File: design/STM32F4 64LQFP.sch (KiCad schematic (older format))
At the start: 15 parts, among them P2 SWD, U1 STM32F40X_LQFP64, X2 8MHz 10ppm

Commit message: Saved project with more recent version of KiCad. Added IRS2184 half bridge driver to BLDC_4_cache.lib
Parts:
- C10, C11, C12, C13, C14, C15, C16, C17, C31, C32, C35, C38: symbol C -> C-RESCUE-BLDC_4
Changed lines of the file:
@@
 EESchema Schematic File Version 2
+LIBS:BLDC_4-rescue
 LIBS:power
 LIBS:device
@@
 LIBS:crf_1
 LIBS:BLDC_4-cache
-EELAYER 24 0
+EELAYER 25 0
 EELAYER END
 $Descr A4 11693 8268
@@
 $EndComp
 $Comp
-L C C17
+L C-RESCUE-BLDC_4 C17
 U 1 1 53F757AE
 P 7500 6350
@@
 $EndComp
 $Comp
-L C C16
+L C-RESCUE-BLDC_4 C16
 U 1 1 53F757B5
 P 7500 6100
@@
 $EndComp
 $Comp
-L GND #PWR035
+L GND-RESCUE-BLDC_4 #PWR035
 U 1 1 53F757BC
 P 8000 6050
@@
 $EndComp
 $Comp
-L GND #PWR037
+L GND-RESCUE-BLDC_4 #PWR037
 U 1 1 53F757C8
 P 7200 5150
@@
 $EndComp
 $Comp
-L C C15
+L C-RESCUE-BLDC_4 C15
 U 1 1 53F757DB
 P 7350 1800
@@
 $EndComp
 $Comp
-L C C38
+L C-RESCUE-BLDC_4 C38
 U 1 1 53F757E2
 P 8100 1800
@@
 $EndComp
 $Comp
-L GND #PWR039
+L GND-RESCUE-BLDC_4 #PWR039
 U 1 1 53F757E9
 P 8250 1600
@@
 $EndComp
 $Comp
-L GND #PWR040
+L GND-RESCUE-BLDC_4 #PWR040
 U 1 1 53F757EF
 P 7150 2550
@@
 SWCLK
 $Comp
-L C C31
+L C-RESCUE-BLDC_4 C31
 U 1 1 53F757F8
 P 7750 5450
@@
 $EndComp
 $Comp
-L C C35
+L C-RESCUE-BLDC_4 C35
 U 1 1 53F757FF
 P 8000 5450
@@
 NoConn ~ 4500 5450
 $Comp
-L GND #PWR042
+L GND-RESCUE-BLDC_4 #PWR042
 U 1 1 53F75856
 P 7950 3300
@@
 	7750 6350 7700 6350
 $Comp
-L C C32
+L C-RESCUE-BLDC_4 C32
 U 1 1 53F75896
 P 7950 3100
@@
 $EndComp
 $Comp
-L GND #PWR044
+L GND-RESCUE-BLDC_4 #PWR044
 U 1 1 53F7741D
 P 9600 3100
@@
 NRST
 $Comp
-L C C10
+L C-RESCUE-BLDC_4 C10
 U 1 1 53F77426
 P 9400 1300
@@
 $EndComp
 $Comp
-L C C11
+L C-RESCUE-BLDC_4 C11
 U 1 1 53F7742D
 P 9650 1300
@@
 $EndComp
 $Comp
-L C C14
+L C-RESCUE-BLDC_4 C14
 U 1 1 53F77434
 P 10400 1300
@@
 $EndComp
 $Comp
-L GND #PWR045
+L GND-RESCUE-BLDC_4 #PWR045
 U 1 1 53F7743B
 P 9100 1650
@@
 $EndComp
 $Comp
-L C C12
+L C-RESCUE-BLDC_4 C12
 U 1 1 53F77447
 P 9900 1300
@@
 $EndComp
 $Comp
-L C C13
+L C-RESCUE-BLDC_4 C13
 U 1 1 53F7744E
 P 10150 1300
@@
 $EndComp
 $Comp
-L GND #PWR047
+L GND-RESCUE-BLDC_4 #PWR047
 U 1 1 54097D19
 P 7750 2150

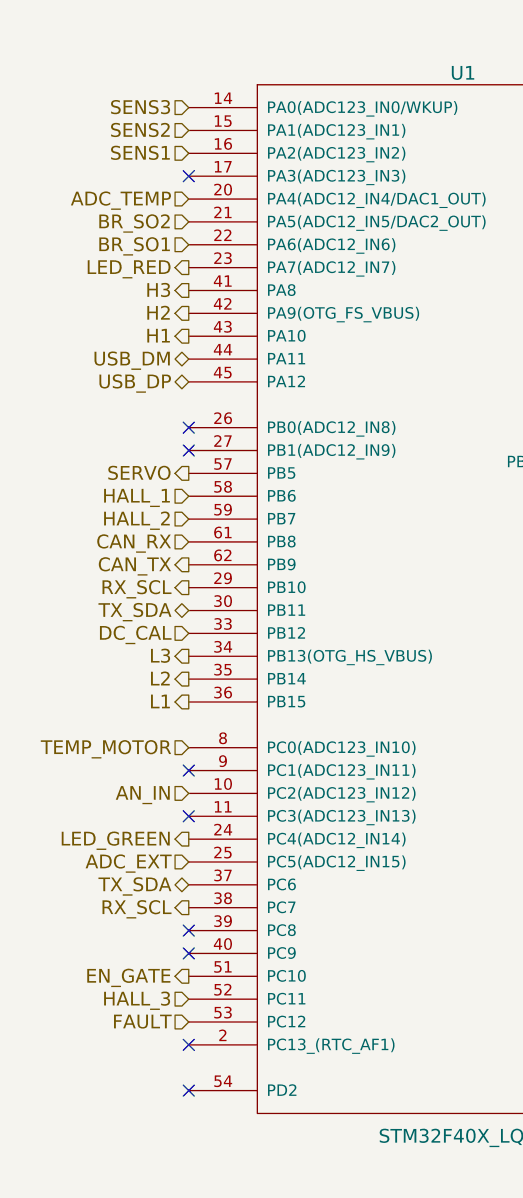
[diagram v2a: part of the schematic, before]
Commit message: Added new drivers and removed the big old one.
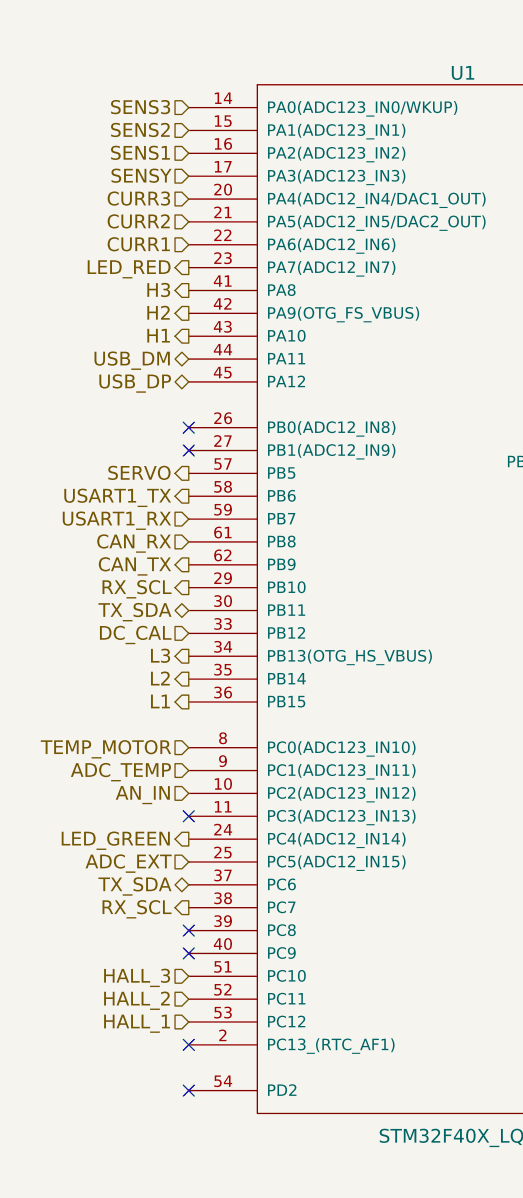
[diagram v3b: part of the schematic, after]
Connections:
- net EN_GATE is gone; now on net HALL_3: U1.51 (PC10)
- net FAULT is gone; now on net HALL_1: U1.53 (PC12)
- net ADC_TEMP: now also U1.9 (PC1(ADC123_IN11)); no longer U1.20 (PA4(ADC12_IN4/DAC1_OUT))
- net HALL_1: no longer U1.58 (PB6)
- net HALL_2: now also U1.52 (PC11); no longer U1.59 (PB7)
- net HALL_3: no longer U1.52 (PC11)
- net SENSY: now reaches U1.17 (PA3(ADC123_IN3))
- net BR_SO1 renamed CURR1
- net BR_SO2 renamed CURR2
- new net CURR3: U1.20 (PA4(ADC12_IN4/DAC1_OUT))
- new net USART1_RX: U1.59 (PB7)
- new net USART1_TX: U1.58 (PB6)
- no-connect marks 16 -> 14
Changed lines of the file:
@@
 $Descr A4 11693 8268
 encoding utf-8
-Sheet 6 8
+Sheet 6 10
 Title "BLDC Driver 4.6"
 Date "25 Aug 2014"
@@
 $EndComp
 NoConn ~ 7000 3300
-NoConn ~ 4500 2050
-NoConn ~ 4500 4650
 NoConn ~ 4500 4850
 $Comp
@@
 Text HLabel 4500 3350 0    60   Output ~ 0
 SERVO
-Text HLabel 4500 3450 0    60   Input ~ 0
+Text HLabel 4500 5750 0    60   Input ~ 0
 HALL_1
-Text HLabel 4500 3550 0    60   Input ~ 0
-HALL_2
 Text HLabel 4500 5650 0    60   Input ~ 0
+HALL_2
+Text HLabel 4500 5550 0    60   Input ~ 0
 HALL_3
 Text HLabel 4500 3850 0    60   Output ~ 0
@@
 Text HLabel 4500 5250 0    60   Output ~ 0
 RX_SCL
-Text HLabel 4500 5750 0    60   Input ~ 0
-FAULT
 Text HLabel 4500 2550 0    60   Output ~ 0
 H3
@@
 SENS1
 Text HLabel 4500 2350 0    60   Input ~ 0
-BR_SO1
+CURR1
 Text HLabel 4500 2250 0    60   Input ~ 0
-BR_SO2
+CURR2
 Text HLabel 4500 4750 0    60   Input ~ 0
 AN_IN
-Text HLabel 4500 5550 0    60   Output ~ 0
-EN_GATE
 Text HLabel 4500 4050 0    60   Input ~ 0
 DC_CAL
@@
 	1    0    0    -1
 $EndComp
-Text HLabel 4500 2150 0    60   Input ~ 0
+Text HLabel 4500 4650 0    60   Input ~ 0
 ADC_TEMP
+Text HLabel 4500 2050 0    60   Input ~ 0
+SENSY
+Text HLabel 4500 2150 0    60   Input ~ 0
+CURR3
+Text HLabel 4500 3450 0    60   Output ~ 0
+USART1_TX
+Text HLabel 4500 3550 0    60   Input ~ 0
+USART1_RX
 $EndSCHEMATC

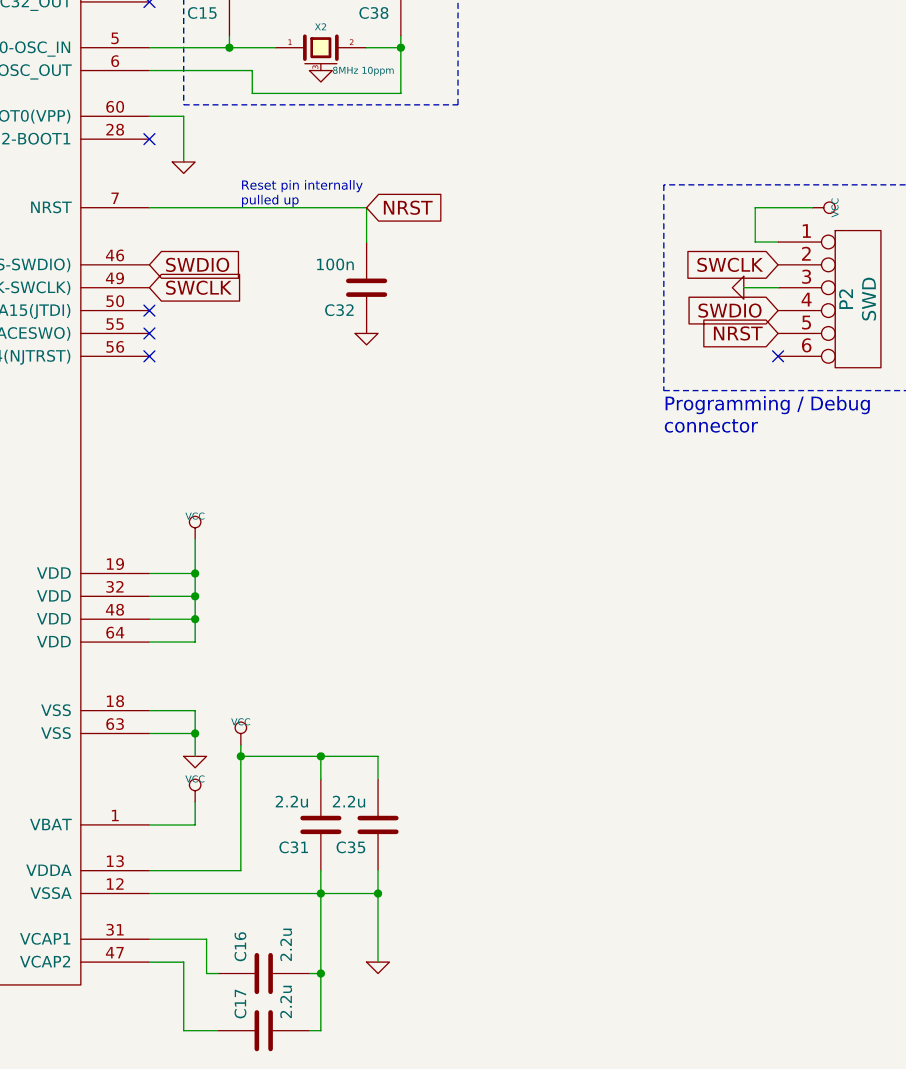
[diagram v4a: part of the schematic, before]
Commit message: First complete draft of the schematics.
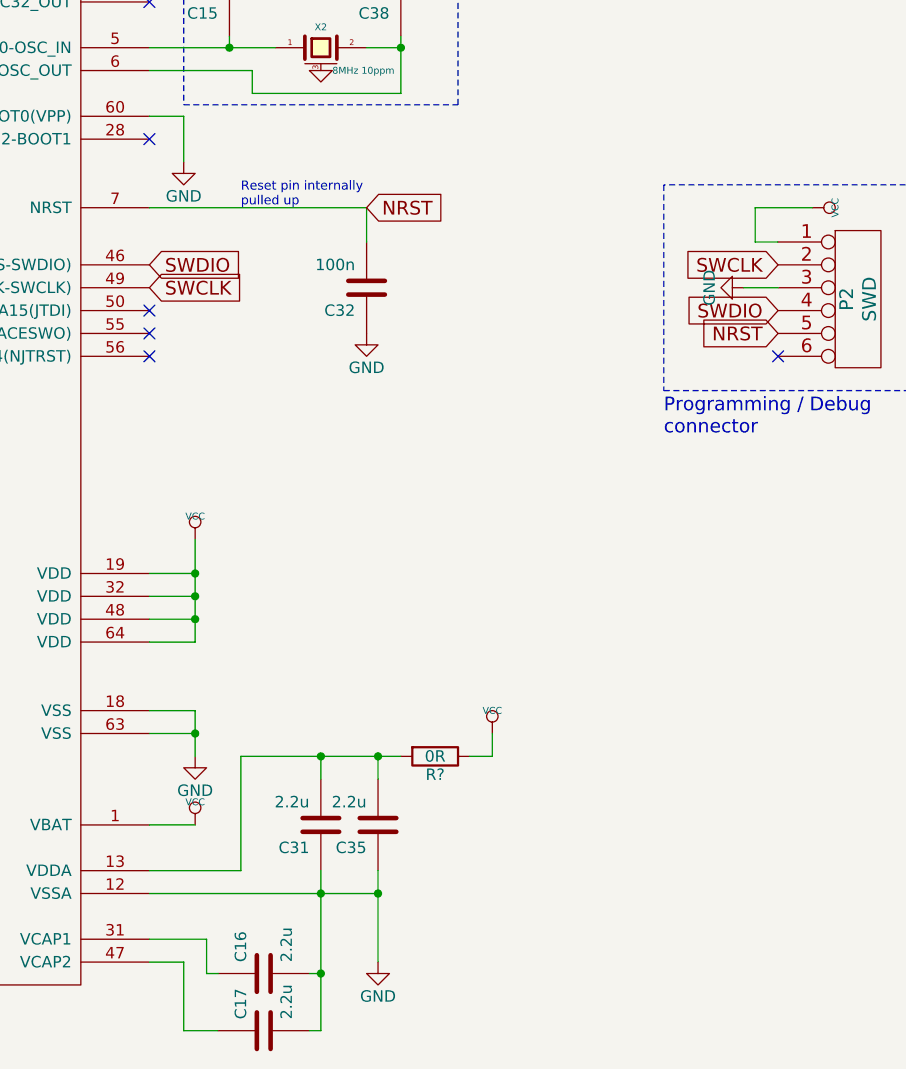
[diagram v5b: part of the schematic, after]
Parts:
- added R?: 0R, symbol R
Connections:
- net VCC: now also R?.1; no longer C31.2, C35.2, U1.13 (VDDA)
- new net: C31.2, C35.2, R?.2, U1.13 (VDDA)
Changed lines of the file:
@@
 $Descr A4 11693 8268
 encoding utf-8
-Sheet 5 10
-Title "BLDC Driver 4.6"
-Date "25 Aug 2014"
-Rev "4.6"
-Comp "Benjamin Vedder"
+Sheet 5 11
+Title "3-Phase Universal Driver"
+Date "2015-08-27"
+Rev "0.1"
+Comp "Jörg Wangemann"
 Comment1 ""
 Comment2 ""
@@
 $EndComp
 $Comp
-L GND-RESCUE-BLDC_4 #PWR035
-U 1 1 53F757BC
-P 8000 6050
-F 0 "#PWR035" H 8000 6050 30  0001 C CNN
-F 1 "GND" H 8000 5980 30  0001 C CNN
-F 2 "" H 8000 6050 60  0001 C CNN
-F 3 "" H 8000 6050 60  0001 C CNN
-	1    8000 6050
-	1    0    0    -1
-$EndComp
-$Comp
 L VCC #PWR036
 U 1 1 53F757C2
-P 7400 5100
-F 0 "#PWR036" H 7400 5200 30  0001 C CNN
-F 1 "VCC" H 7400 5200 30  0000 C CNN
-F 2 "" H 7400 5100 60  0001 C CNN
-F 3 "" H 7400 5100 60  0001 C CNN
-	1    7400 5100
-	1    0    0    -1
-$EndComp
-$Comp
-L GND-RESCUE-BLDC_4 #PWR037
-U 1 1 53F757C8
-P 7200 5150
-F 0 "#PWR037" H 7200 5150 30  0001 C CNN
-F 1 "GND" H 7200 5080 30  0001 C CNN
-F 2 "" H 7200 5150 60  0001 C CNN
-F 3 "" H 7200 5150 60  0001 C CNN
-	1    7200 5150
+P 8500 5050
+F 0 "#PWR036" H 8500 5150 30  0001 C CNN
+F 1 "VCC" H 8500 5150 30  0000 C CNN
+F 2 "" H 8500 5050 60  0001 C CNN
+F 3 "" H 8500 5050 60  0001 C CNN
+	1    8500 5050
 	1    0    0    -1
 $EndComp
@@
 	1    0    0    -1
 $EndComp
-$Comp
-L GND-RESCUE-BLDC_4 #PWR040
-U 1 1 53F757EF
-P 7150 2550
-F 0 "#PWR040" H 7150 2550 30  0001 C CNN
-F 1 "GND" H 7150 2480 30  0001 C CNN
-F 2 "" H 7150 2550 60  0001 C CNN
-F 3 "" H 7150 2550 60  0001 C CNN
-	1    7150 2550
-	1    0    0    -1
-$EndComp
 Text GLabel 7000 3000 2    60   Input ~ 0
 SWDIO
@@
 L VCC #PWR041
 U 1 1 53F75807
-P 7200 5350
-F 0 "#PWR041" H 7200 5450 30  0001 C CNN
-F 1 "VCC" H 7200 5450 30  0000 C CNN
-F 2 "" H 7200 5350 60  0001 C CNN
-F 3 "" H 7200 5350 60  0001 C CNN
-	1    7200 5350
+P 7200 5450
+F 0 "#PWR041" H 7200 5550 30  0001 C CNN
+F 1 "VCC" H 7200 5550 30  0000 C CNN
+F 2 "" H 7200 5450 60  0001 C CNN
+F 3 "" H 7200 5450 60  0001 C CNN
+	1    7200 5450
 	1    0    0    -1
 $EndComp
@@
 NoConn ~ 4500 3150
 NoConn ~ 4500 5450
-$Comp
-L GND-RESCUE-BLDC_4 #PWR042
-U 1 1 53F75856
-P 7950 3300
-F 0 "#PWR042" H 7950 3300 30  0001 C CNN
-F 1 "GND" H 7950 3230 30  0001 C CNN
-F 2 "" H 7950 3300 60  0001 C CNN
-F 3 "" H 7950 3300 60  0001 C CNN
-	1    7950 3300
-	1    0    0    -1
-$EndComp
 Wire Wire Line
 	7950 3300 7950 3300
 Wire Wire Line
-	7200 5450 7200 5350
-Wire Wire Line
 	7000 5450 7200 5450
 Connection ~ 8000 5750
@@
 Wire Wire Line
 	8000 5150 8000 5250
-Connection ~ 7400 5150
 Wire Wire Line
-	7400 5150 8000 5150
+	7400 5150 8100 5150
 Wire Wire Line
 	7750 5250 7750 5150
@@
 Wire Wire Line
 	7200 4950 7200 5150
-Wire Wire Line
-	7400 5100 7400 5650
 Connection ~ 7750 5750
 Wire Wire Line
@@
 	0    1    1    0
 $EndComp
-$Comp
-L GND-RESCUE-BLDC_4 #PWR044
-U 1 1 53F7741D
-P 9600 3100
-F 0 "#PWR044" H 9600 3100 30  0001 C CNN
-F 1 "GND" H 9600 3030 30  0001 C CNN
-F 2 "" H 9600 3100 60  0001 C CNN
-F 3 "" H 9600 3100 60  0001 C CNN
-	1    9600 3100
-	0    1    1    0
-$EndComp
 Text GLabel 9750 3000 0    60   Input ~ 0
 SWCLK
@@
 Text HLabel 4500 3550 0    60   Input ~ 0
 USART1_RX
+$Comp
+L GND #PWR?
+U 1 1 55E72202
+P 7150 2550
+F 0 "#PWR?" H 7150 2300 50  0001 C CNN
+F 1 "GND" H 7150 2400 50  0000 C CNN
+F 2 "" H 7150 2550 60  0000 C CNN
+F 3 "" H 7150 2550 60  0000 C CNN
+	1    7150 2550
+	1    0    0    -1
+$EndComp
+$Comp
+L GND #PWR?
+U 1 1 55E72244
+P 7950 3300
+F 0 "#PWR?" H 7950 3050 50  0001 C CNN
+F 1 "GND" H 7950 3150 50  0000 C CNN
+F 2 "" H 7950 3300 60  0000 C CNN
+F 3 "" H 7950 3300 60  0000 C CNN
+	1    7950 3300
+	1    0    0    -1
+$EndComp
+$Comp
+L GND #PWR?
+U 1 1 55E72286
+P 9600 3100
+F 0 "#PWR?" H 9600 2850 50  0001 C CNN
+F 1 "GND" H 9600 2950 50  0000 C CNN
+F 2 "" H 9600 3100 60  0000 C CNN
+F 3 "" H 9600 3100 60  0000 C CNN
+	1    9600 3100
+	0    1    1    0
+$EndComp
+$Comp
+L GND #PWR?
+U 1 1 55E72368
+P 7200 5150
+F 0 "#PWR?" H 7200 4900 50  0001 C CNN
+F 1 "GND" H 7200 5000 50  0000 C CNN
+F 2 "" H 7200 5150 60  0000 C CNN
+F 3 "" H 7200 5150 60  0000 C CNN
+	1    7200 5150
+	1    0    0    -1
+$EndComp
+$Comp
+L GND #PWR?
+U 1 1 55E723AA
+P 8000 6050
+F 0 "#PWR?" H 8000 5800 50  0001 C CNN
+F 1 "GND" H 8000 5900 50  0000 C CNN
+F 2 "" H 8000 6050 60  0000 C CNN
+F 3 "" H 8000 6050 60  0000 C CNN
+	1    8000 6050
+	1    0    0    -1
+$EndComp
+Wire Wire Line
+	7400 5150 7400 5650
+$Comp
+L R R?
+U 1 1 55E738BB
+P 8250 5150
+F 0 "R?" V 8330 5150 50  0000 C CNN
+F 1 "0R" V 8250 5150 50  0000 C CNN
+F 2 "" V 8180 5150 30  0000 C CNN
+F 3 "" H 8250 5150 30  0000 C CNN
+	1    8250 5150
+	0    1    1    0
+$EndComp
+Connection ~ 8000 5150
+Wire Wire Line
+	8500 5050 8500 5150
+Wire Wire Line
+	8500 5150 8400 5150
 $EndSCHEMATC
